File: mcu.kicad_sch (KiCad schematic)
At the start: 16 parts, among them J1 Conn_ARM_SWD_TagConnect_TC2030, U2 STM32L053R8Tx

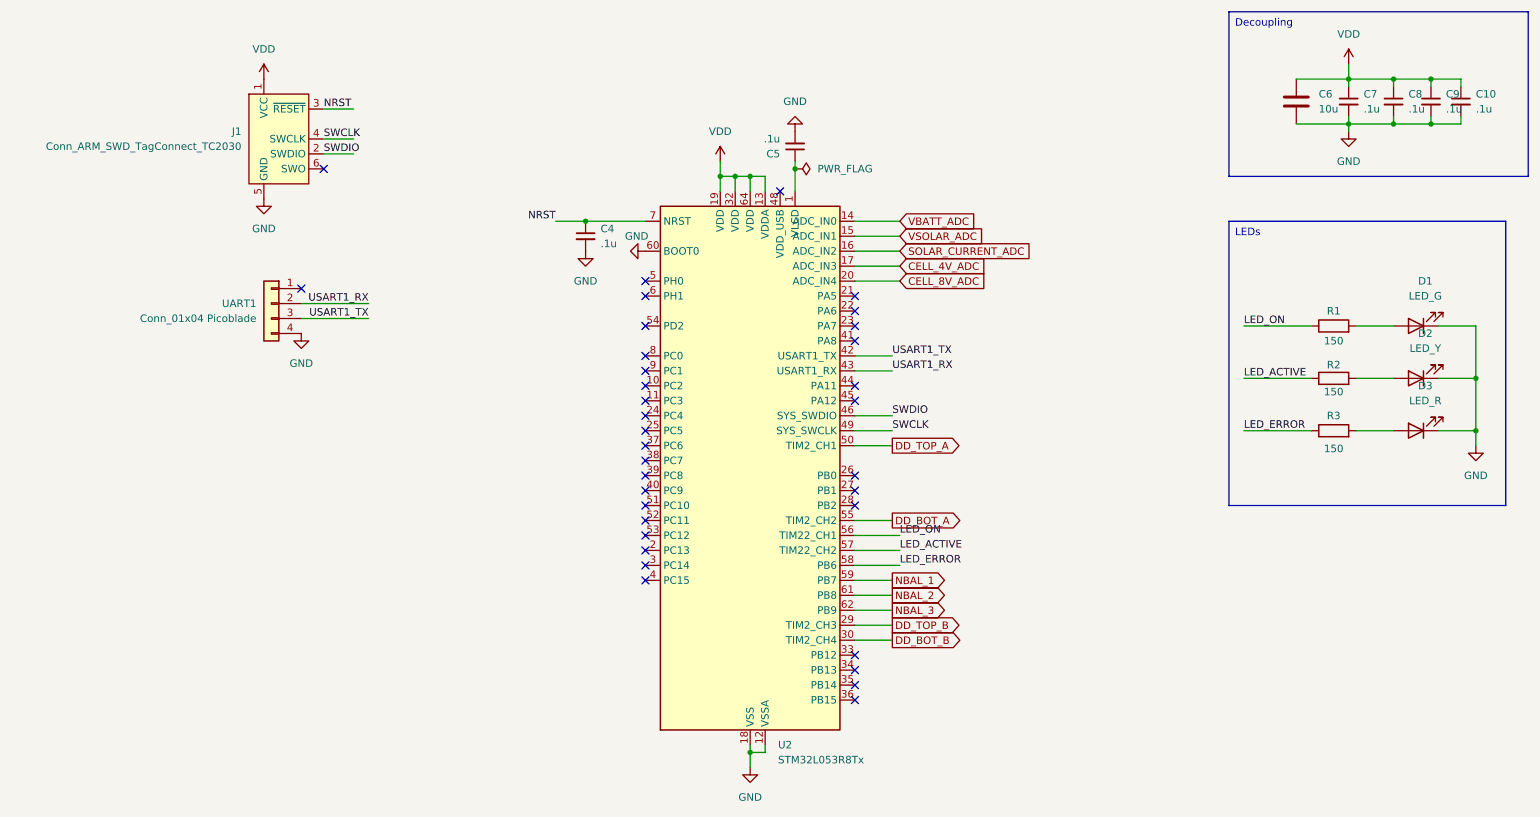
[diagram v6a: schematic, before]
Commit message: Better balance resistors, fixes
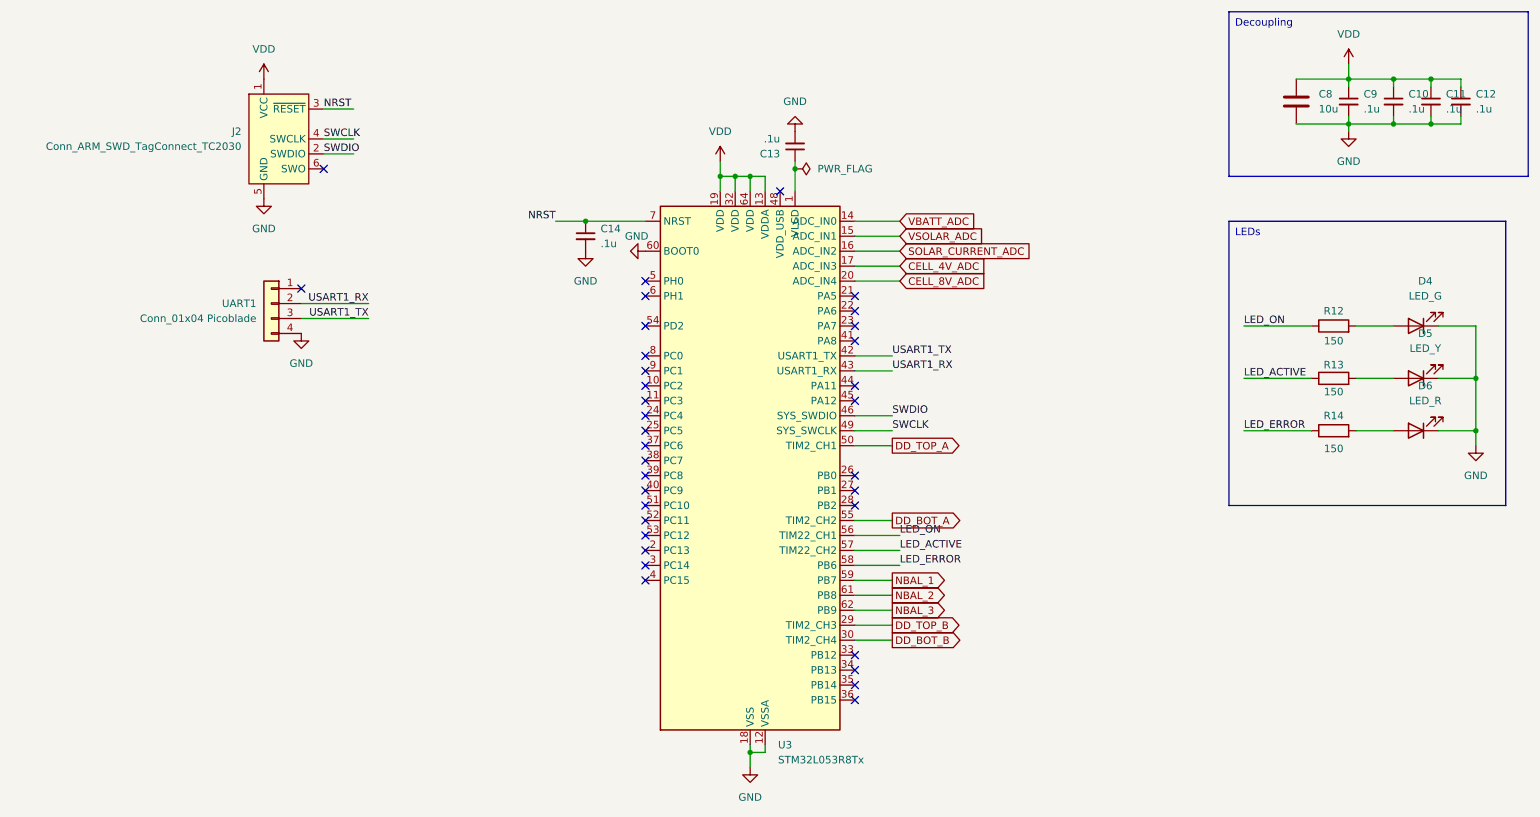
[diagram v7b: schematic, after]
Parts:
- renumbered C8 to C10, C9 to C11, C10 to C12, C5 to C13, C4 to C14, C6 to C8, C7 to C9, D1 to D4, D2 to D5, D3 to D6, J1 to J2, R1 to R12, R2 to R13, R3 to R14, U2 to U3
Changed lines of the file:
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@@
 		(dnp no)
 		(fields_autoplaced yes)
-		(property "Reference" "C8"
+		(property "Reference" "C10"
 			(at 252.73 29.2162 0)
 			(effects
@@
 			(project "JPBms2"
 				(path "/d86e471c-a8be-422d-a5d1-5a4699b7b766/852788cb-2266-4d4a-865c-a7e0873e4190"
-					(reference "C8")
+					(reference "C10")
 					(unit 1)
 				)
@@
 		(dnp no)
 		(fields_autoplaced yes)
-		(property "Reference" "#PWR012"
+		(property "Reference" "#PWR022"
 			(at 242.57 41.91 0)
 			(effects
@@
 			(project "JPBms2"
 				(path "/d86e471c-a8be-422d-a5d1-5a4699b7b766/852788cb-2266-4d4a-865c-a7e0873e4190"
-					(reference "#PWR012")
+					(reference "#PWR022")
 					(unit 1)
 				)
@@
 		(dnp no)
 		(fields_autoplaced yes)
-		(property "Reference" "#PWR08"
+		(property "Reference" "#PWR027"
 			(at 64.77 76.2 0)
 			(effects
@@
 			(project "JPBms2"
 				(path "/d86e471c-a8be-422d-a5d1-5a4699b7b766/852788cb-2266-4d4a-865c-a7e0873e4190"
-					(reference "#PWR08")
+					(reference "#PWR027")
 					(unit 1)
 				)
@@
 		(dnp no)
 		(fields_autoplaced yes)
-		(property "Reference" "D3"
+		(property "Reference" "D6"
 			(at 255.5875 78.74 0)
 			(effects
@@
 			(project "JPBms2"
 				(path "/d86e471c-a8be-422d-a5d1-5a4699b7b766/852788cb-2266-4d4a-865c-a7e0873e4190"
-					(reference "D3")
+					(reference "D6")
 					(unit 1)
 				)
@@
 		(dnp no)
 		(fields_autoplaced yes)
-		(property "Reference" "#PWR011"
+		(property "Reference" "#PWR021"
 			(at 148.59 29.21 0)
 			(effects
@@
 			(project "JPBms2"
 				(path "/d86e471c-a8be-422d-a5d1-5a4699b7b766/852788cb-2266-4d4a-865c-a7e0873e4190"
-					(reference "#PWR011")
+					(reference "#PWR021")
 					(unit 1)
 				)
@@
 		(on_board yes)
 		(dnp no)
-		(property "Reference" "#PWR013"
+		(property "Reference" "#PWR019"
 			(at 242.57 27.94 0)
 			(effects
@@
 			(project "JPBms2"
 				(path "/d86e471c-a8be-422d-a5d1-5a4699b7b766/852788cb-2266-4d4a-865c-a7e0873e4190"
-					(reference "#PWR013")
+					(reference "#PWR019")
 					(unit 1)
 				)
@@
 		(dnp no)
 		(fields_autoplaced yes)
-		(property "Reference" "C6"
+		(property "Reference" "C8"
 			(at 237.49 29.2099 0)
 			(effects
@@
 			(project "JPBms2"
 				(path "/d86e471c-a8be-422d-a5d1-5a4699b7b766/852788cb-2266-4d4a-865c-a7e0873e4190"
-					(reference "C6")
+					(reference "C8")
 					(unit 1)
 				)
@@
 		(dnp no)
 		(fields_autoplaced yes)
-		(property "Reference" "U2"
+		(property "Reference" "U3"
 			(at 145.7041 139.7 0)
 			(effects
@@
 			(project "JPBms2"
 				(path "/d86e471c-a8be-422d-a5d1-5a4699b7b766/852788cb-2266-4d4a-865c-a7e0873e4190"
-					(reference "U2")
+					(reference "U3")
 					(unit 1)
 				)
@@
 		(dnp no)
 		(fields_autoplaced yes)
-		(property "Reference" "C9"
+		(property "Reference" "C11"
 			(at 259.08 29.2162 0)
 			(effects
@@
 			(project "JPBms2"
 				(path "/d86e471c-a8be-422d-a5d1-5a4699b7b766/852788cb-2266-4d4a-865c-a7e0873e4190"
-					(reference "C9")
+					(reference "C11")
 					(unit 1)
 				)
@@
 		(dnp no)
 		(fields_autoplaced yes)
-		(property "Reference" "#PWR04"
+		(property "Reference" "#PWR023"
 			(at 135.89 44.45 0)
 			(effects
@@
 			(project "JPBms2"
 				(path "/d86e471c-a8be-422d-a5d1-5a4699b7b766/852788cb-2266-4d4a-865c-a7e0873e4190"
-					(reference "#PWR04")
+					(reference "#PWR023")
 					(unit 1)
 				)
@@
 		(dnp no)
 		(fields_autoplaced yes)
-		(property "Reference" "C4"
+		(property "Reference" "C14"
 			(at 115.57 52.0762 0)
 			(effects
@@
 			(project "JPBms2"
 				(path "/d86e471c-a8be-422d-a5d1-5a4699b7b766/852788cb-2266-4d4a-865c-a7e0873e4190"
-					(reference "C4")
+					(reference "C14")
 					(unit 1)
 				)
@@
 		(dnp no)
 		(fields_autoplaced yes)
-		(property "Reference" "C7"
+		(property "Reference" "C9"
 			(at 245.11 29.2162 0)
 			(effects
@@
 			(project "JPBms2"
 				(path "/d86e471c-a8be-422d-a5d1-5a4699b7b766/852788cb-2266-4d4a-865c-a7e0873e4190"
-					(reference "C7")
+					(reference "C9")
 					(unit 1)
 				)
@@
 		(dnp no)
 		(fields_autoplaced yes)
-		(property "Reference" "D1"
+		(property "Reference" "D4"
 			(at 255.5875 60.96 0)
 			(effects
@@
 			(project "JPBms2"
 				(path "/d86e471c-a8be-422d-a5d1-5a4699b7b766/852788cb-2266-4d4a-865c-a7e0873e4190"
-					(reference "D1")
+					(reference "D4")
 					(unit 1)
 				)
@@
 		(dnp no)
 		(fields_autoplaced yes)
-		(property "Reference" "C10"
+		(property "Reference" "C12"
 			(at 264.16 29.2162 0)
 			(effects
@@
 			(project "JPBms2"
 				(path "/d86e471c-a8be-422d-a5d1-5a4699b7b766/852788cb-2266-4d4a-865c-a7e0873e4190"
-					(reference "C10")
+					(reference "C12")
 					(unit 1)
 				)
@@
 		(dnp no)
 		(fields_autoplaced yes)
-		(property "Reference" "#PWR07"
+		(property "Reference" "#PWR020"
 			(at 58.42 30.48 0)
 			(effects
@@
 			(project "JPBms2"
 				(path "/d86e471c-a8be-422d-a5d1-5a4699b7b766/852788cb-2266-4d4a-865c-a7e0873e4190"
-					(reference "#PWR07")
+					(reference "#PWR020")
 					(unit 1)
 				)
@@
 		(dnp no)
 		(fields_autoplaced yes)
-		(property "Reference" "#PWR015"
+		(property "Reference" "#PWR028"
 			(at 264.16 95.25 0)
 			(effects
@@
 			(project "JPBms2"
 				(path "/d86e471c-a8be-422d-a5d1-5a4699b7b766/852788cb-2266-4d4a-865c-a7e0873e4190"
-					(reference "#PWR015")
+					(reference "#PWR028")
 					(unit 1)
 				)
@@
 		(dnp no)
 		(fields_autoplaced yes)
-		(property "Reference" "C5"
+		(property "Reference" "C13"
 			(at 146.05 39.3638 0)
 			(effects
@@
 			(project "JPBms2"
 				(path "/d86e471c-a8be-422d-a5d1-5a4699b7b766/852788cb-2266-4d4a-865c-a7e0873e4190"
-					(reference "C5")
+					(reference "C13")
 					(unit 1)
 				)
@@
 		(dnp no)
 		(fields_autoplaced yes)
-		(property "Reference" "#PWR010"
+		(property "Reference" "#PWR025"
 			(at 113.03 62.23 0)
 			(effects
@@
 			(project "JPBms2"
 				(path "/d86e471c-a8be-422d-a5d1-5a4699b7b766/852788cb-2266-4d4a-865c-a7e0873e4190"
-					(reference "#PWR010")
+					(reference "#PWR025")
 					(unit 1)
 				)
@@
 		(dnp no)
 		(fields_autoplaced yes)
-		(property "Reference" "D2"
+		(property "Reference" "D5"
 			(at 255.5875 69.85 0)
 			(effects
@@
 			(project "JPBms2"
 				(path "/d86e471c-a8be-422d-a5d1-5a4699b7b766/852788cb-2266-4d4a-865c-a7e0873e4190"
-					(reference "D2")
+					(reference "D5")
 					(unit 1)
 				)
@@
 		(dnp no)
 		(fields_autoplaced yes)
-		(property "Reference" "#PWR06"
+		(property "Reference" "#PWR024"
 			(at 58.42 53.34 0)
 			(effects
@@
 			(project "JPBms2"
 				(path "/d86e471c-a8be-422d-a5d1-5a4699b7b766/852788cb-2266-4d4a-865c-a7e0873e4190"
-					(reference "#PWR06")
+					(reference "#PWR024")
 					(unit 1)
 				)
@@
 		(dnp no)
 		(fields_autoplaced yes)
-		(property "Reference" "#PWR05"
+		(property "Reference" "#PWR029"
 			(at 140.97 149.86 0)
 			(effects
@@
 			(project "JPBms2"
 				(path "/d86e471c-a8be-422d-a5d1-5a4699b7b766/852788cb-2266-4d4a-865c-a7e0873e4190"
-					(reference "#PWR05")
+					(reference "#PWR029")
 					(unit 1)
 				)
@@
 		(dnp no)
 		(fields_autoplaced yes)
-		(property "Reference" "J1"
+		(property "Reference" "J2"
 			(at 54.61 35.5599 0)
 			(effects
@@
 			(project "JPBms2"
 				(path "/d86e471c-a8be-422d-a5d1-5a4699b7b766/852788cb-2266-4d4a-865c-a7e0873e4190"
-					(reference "J1")
+					(reference "J2")
 					(unit 1)
 				)
@@
 		(on_board yes)
 		(dnp no)
-		(property "Reference" "R3"
+		(property "Reference" "R14"
 			(at 240.03 83.82 90)
 			(effects
@@
 			(project "JPBms2"
 				(path "/d86e471c-a8be-422d-a5d1-5a4699b7b766/852788cb-2266-4d4a-865c-a7e0873e4190"
-					(reference "R3")
+					(reference "R14")
 					(unit 1)
 				)
@@
 		(on_board yes)
 		(dnp no)
-		(property "Reference" "#PWR014"
+		(property "Reference" "#PWR026"
 			(at 116.84 55.88 0)
 			(effects
@@
 			(project "JPBms2"
 				(path "/d86e471c-a8be-422d-a5d1-5a4699b7b766/852788cb-2266-4d4a-865c-a7e0873e4190"
-					(reference "#PWR014")
+					(reference "#PWR026")
 					(unit 1)
 				)
@@
 		(on_board yes)
 		(dnp no)
-		(property "Reference" "R1"
+		(property "Reference" "R12"
 			(at 240.03 66.04 90)
 			(effects
@@
 			(project "JPBms2"
 				(path "/d86e471c-a8be-422d-a5d1-5a4699b7b766/852788cb-2266-4d4a-865c-a7e0873e4190"
-					(reference "R1")
+					(reference "R12")
 					(unit 1)
 				)
@@
 		(on_board yes)
 		(dnp no)
-		(property "Reference" "R2"
+		(property "Reference" "R13"
 			(at 240.03 75.184 90)
 			(effects
@@
 			(project "JPBms2"
 				(path "/d86e471c-a8be-422d-a5d1-5a4699b7b766/852788cb-2266-4d4a-865c-a7e0873e4190"
-					(reference "R2")
-					(unit 1)
-				)
+					(reference "R13")
+					(unit 1)
+				)

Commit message: V1.1 spin
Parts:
- added C21: .1u, Capacitor_SMD:C_0603_1608Metric, symbol Device:C_Small
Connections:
- net GND: now also C21.2
- net VDD: now also U3.48 (VDD_USB), C21.1
- no-connect marks 35 -> 34
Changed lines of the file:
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@@
 	)
 	(junction
+		(at 143.51 43.18)
+		(diameter 0)
+		(color 0 0 0 0)
+	)
+	(junction
+		(at 261.62 26.67)
+		(diameter 0)
+		(color 0 0 0 0)
+	)
+	(junction
 		(at 138.43 43.18)
 		(diameter 0)
@@
 	)
 	(junction
+		(at 261.62 34.29)
+		(diameter 0)
+		(color 0 0 0 0)
+	)
+	(junction
 		(at 135.89 43.18)
 		(diameter 0)
@@
 	)
 	(no_connect
-		(at 146.05 45.72)
-	)
-	(no_connect
 		(at 158.75 129.54)
 	)
@@
 	(wire
 		(pts
+			(xy 146.05 45.72) (xy 146.05 43.18)
+		)
+		(stroke
+			(width 0)
+			(type default)
+		)
+	)
+	(wire
+		(pts
 			(xy 224.79 68.58) (xy 236.22 68.58)
 		)
@@
 	(wire
 		(pts
+			(xy 146.05 43.18) (xy 143.51 43.18)
+		)
+		(stroke
+			(width 0)
+			(type default)
+		)
+	)
+	(wire
+		(pts
 			(xy 261.62 26.67) (xy 261.62 27.94)
 		)
@@
 	(wire
 		(pts
+			(xy 265.43 26.67) (xy 261.62 26.67)
+		)
+		(stroke
+			(width 0)
+			(type default)
+		)
+	)
+	(wire
+		(pts
 			(xy 256.54 33.02) (xy 256.54 34.29)
 		)
@@
 	(wire
 		(pts
+			(xy 265.43 27.94) (xy 265.43 26.67)
+		)
+		(stroke
+			(width 0)
+			(type default)
+		)
+	)
+	(wire
+		(pts
 			(xy 165.1 88.9) (xy 158.75 88.9)
 		)
@@
 	(wire
 		(pts
+			(xy 261.62 34.29) (xy 265.43 34.29)
+		)
+		(stroke
+			(width 0)
+			(type default)
+		)
+	)
+	(wire
+		(pts
 			(xy 158.75 116.84) (xy 165.1 116.84)
 		)
@@
 	(wire
 		(pts
+			(xy 265.43 34.29) (xy 265.43 33.02)
+		)
+		(stroke
+			(width 0)
+			(type default)
+		)
+	)
+	(wire
+		(pts
 			(xy 166.37 109.22) (xy 158.75 109.22)
 		)
@@
 					(unit 1)
 				)
+			)
+		)
+	)
+	(symbol
+		(lib_id "Device:C_Small")
+		(at 265.43 30.48 0)
+		(unit 1)
+		(exclude_from_sim no)
+		(in_bom yes)
+		(on_board yes)
+		(dnp no)
+		(fields_autoplaced yes)
+		(property "Reference" "C21"
+			(at 267.97 29.2162 0)
+			(effects
+				(font
+					(size 1.27 1.27)
+				)
+				(justify left)
+			)
+		)
+		(property "Value" ".1u"
+			(at 267.97 31.7562 0)
+			(effects
+				(font
+					(size 1.27 1.27)
+				)
+				(justify left)
+			)
+		)
+		(property "Footprint" "Capacitor_SMD:C_0603_1608Metric"
+			(at 265.43 30.48 0)
+			(effects
+				(font
+					(size 1.27 1.27)
+				)
+				(hide yes)
+			)
+		)
+		(property "Datasheet" "~"
+			(at 265.43 30.48 0)
+			(effects
+				(font
+					(size 1.27 1.27)
+				)
+				(hide yes)
+			)
+		)
+		(property "Description" "Unpolarized capacitor, small symbol"
+			(at 265.43 30.48 0)
+			(effects
+				(font
+					(size 1.27 1.27)
+				)
+				(hide yes)
+			)
+		)
+		(property "LCSC_Code" "C14663"
+			(at 265.43 30.48 0)
+			(effects
+				(font
+					(size 1.27 1.27)
+				)
+				(hide yes)
+			)
+		)
+		(pin "2"
+		)
+		(pin "1"
+		)
+		(instances
+			(project "JPBms2"
+				(path "/d86e471c-a8be-422d-a5d1-5a4699b7b766/852788cb-2266-4d4a-865c-a7e0873e4190"
+					(reference "C21")
+					(unit 1)
+				)
